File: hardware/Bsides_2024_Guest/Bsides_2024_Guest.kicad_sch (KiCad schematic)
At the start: 31 parts, among them J1 UART, J2 Battery, J3 OLED, J4 I2C, P1 USB_C_Plug_USB2.0, Q1 DMG3415U-7, SW1 ON, SW2 RESET, SW3 GPIO, SW4 RESET, SW5 RESET, SW6 RESET, SW7 RESET, U1 ESP32-C6-WROOM-1U-N4, U2 AP2112K-3.3

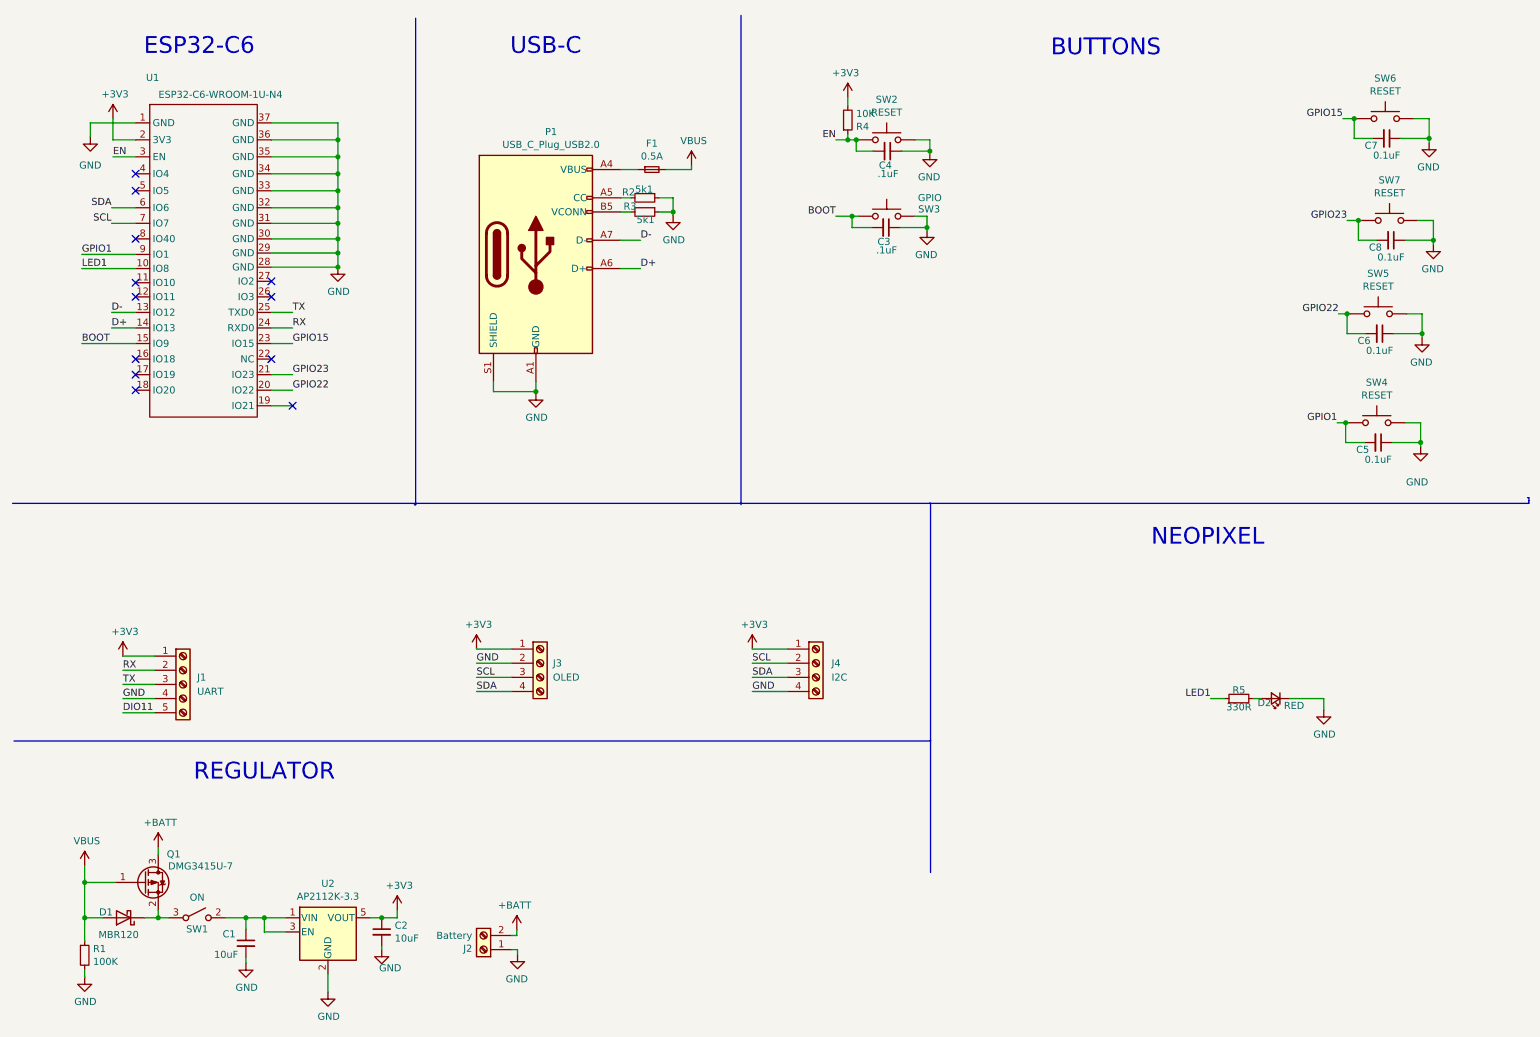
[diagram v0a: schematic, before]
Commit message: feat(Hw):Added_Guest_And_Sponsor_Floorplan_and_3d_Models
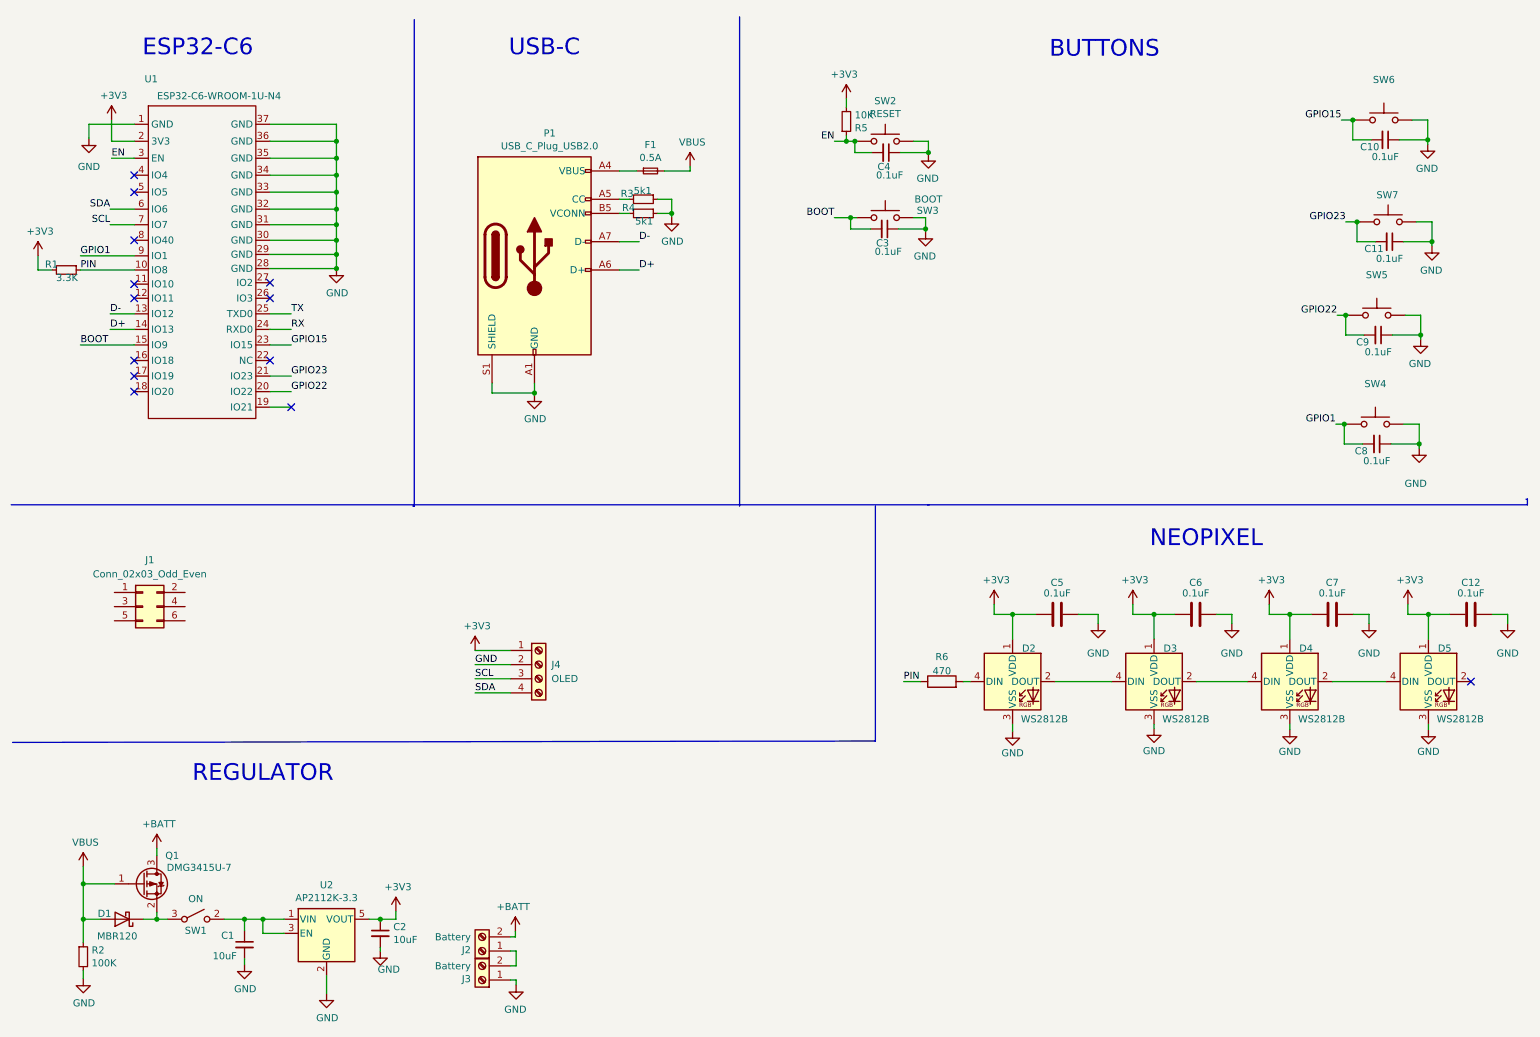
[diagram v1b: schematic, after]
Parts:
- removed C5, C6, C7: 0.1uF, symbol Device:C_Small
- removed D2: RED, LED_SMD:LED_0805_2012Metric, symbol Device:LED_Small
- removed J1: UART, Connector_PinHeader_2.54mm:PinHeader_1x05_P2.54mm_Vertical, symbol Connector:Screw_Terminal_01x05
- removed J3: OLED, Connector_PinHeader_2.54mm:PinHeader_1x04_P2.54mm_Vertical, symbol Connector:Screw_Terminal_01x04
- added C10, C11, C9: 0.1uF, Capacitor_SMD:C_0603_1608Metric, symbol Device:C_Small
- added C12, C5, C6, C7: 0.1uF, Capacitor_SMD:C_0603_1608Metric, symbol Device:C
- added D2, D3, D4, D5: WS2812B, LED_SMD:LED_WS2812B-Mini_PLCC4_3.5x3.5mm, symbol LED:WS2812B
- added J1: Conn_02x03_Odd_Even, Connector_PinSocket_2.54mm:PinSocket_2x03_P2.54mm_Vertical, symbol Connector_Generic:Conn_02x03_Odd_Even
- added J3: Battery, bsides:BH-AAA-A1aj001, symbol Connector:Screw_Terminal_01x02
- added R6: 470, Resistor_SMD:R_0603_1608Metric, symbol Device:R
- C3, C4: value .1uF -> 0.1uF
- C8: footprint (none) -> Capacitor_SMD:C_0603_1608Metric
- J2: footprint Footprint:BAT-TH_BH-AAA-A1AJ024 -> bsides:BH-AAA-A1aj001
- J4: value I2C -> OLED; footprint Connector_PinHeader_2.54mm:PinHeader_1x04_P2.54mm_Vertical -> bsides:Display OLED 128 x32; LCSC# C2691448 -> (none); manf# (none) -> I2C SH1106 Display Oled Azul 128×64 1.3 ”; provedor LCSC -> UNIT Electronics
- P1: footprint Footprint:C393939 -> bsides:C393939
- R1: value 100K -> 3.3K; LCSC# C25803 -> (none); Proveedor LCSC -> (none); provedor LCSC -> (none)
- R2: value 5k1 -> 100K; LCSC# C191782 -> C25803; Proveedor (none) -> LCSC; manf# ERJ3RBD5101V -> (none)
- R4: value 10K -> 5k1; LCSC# C217281 -> C191782; manf# CR-03JL7---10K -> ERJ3RBD5101V
- R5: value 330R -> 10K; footprint Resistor_SMD:R_0805_2012Metric_Pad1.20x1.40mm_HandSolder -> Resistor_SMD:R_0603_1608Metric; LCSC# C119075 -> C217281; manf# (none) -> CR-03JL7---10K
- SW1: footprint Footprint:JS102011SAQN -> bsides:MSK12C02
- SW3: value GPIO -> BOOT
- SW5, SW7: value RESET -> ~
- U1: footprint Footprint:MOD28_ESP32-C6-WROOM-1U_EXP -> bsides:XCVR_ESP32-C6-WROOM-1-N8
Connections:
- net +3V3: now also R1.2, R5.2, C12.2, C5.2, C6.2, C7.2, D2.1 (VDD), D3.1 (VDD), D4.1 (VDD), D5.1 (VDD); no longer R4.2
- net EN: now also R5.1; no longer R4.1
- net GND: now also J4.2 (Pin_2), R2.2, R4.1, C10.1, C11.1, C12.1, C5.1, C6.1, C7.1, C9.1, D2.3 (VSS), D3.3 (VSS), D4.3 (VSS), D5.3 (VSS), J3.1 (Pin_1); no longer J2.1 (Pin_1), J4.4 (Pin_4), R1.2, R2.1
- net GPIO1: now also C8.2
- net GPIO15: now also C10.2
- net GPIO22: now also C9.2
- net GPIO23: now also C11.2; no longer C8.2
- net SCL: now also J4.3 (Pin_3); no longer J4.2 (Pin_2)
- net SDA: now also J4.4 (Pin_4); no longer J4.3 (Pin_3)
- net VBUS: now also R2.1; no longer R1.1
- net at R3.2: now also P1.A5 (CC); no longer P1.B5 (VCONN)
- net LED1 renamed PIN
- net PIN: now also R1.1, R6.1; no longer R5.1
- new net: P1.B5 (VCONN), R4.2
- new net: D3.2 (DOUT), D4.4 (DIN)
- new net: D2.2 (DOUT), D3.4 (DIN)
- new net: J2.1 (Pin_1), J3.2 (Pin_2)
- new net: D4.2 (DOUT), D5.4 (DIN)
- new net: D2.4 (DIN), R6.2
- no-connect marks 12 -> 13

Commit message: feat(Hw): Shitty Addon PCB added
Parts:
- added C13: 1uF, Capacitor_SMD:C_0603_1608Metric, symbol Device:C_Small
- added C14, C15: 10uF, Capacitor_SMD:C_0603_1608Metric, symbol Device:C_Small
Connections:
- net +3V3: now also C13.1, C14.1, C15.1
- net GND: now also C13.2, C14.2, C15.2
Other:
- moved on the sheet: C3, C4, F1, P1, R3, R4, R5, SW2, SW3

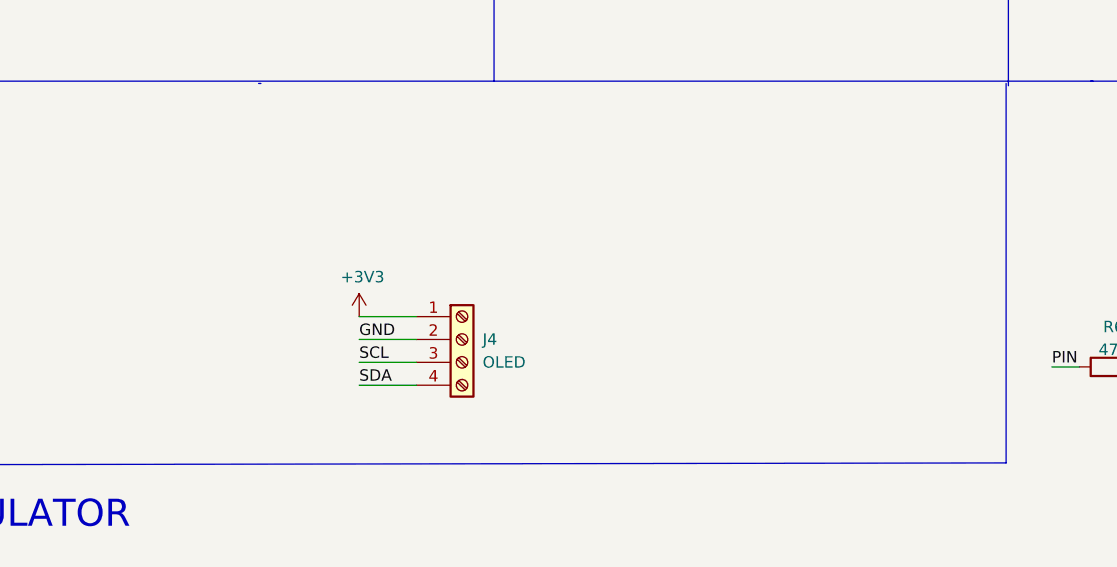
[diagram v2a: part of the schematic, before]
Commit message: feat(Hw): Start new floorplan
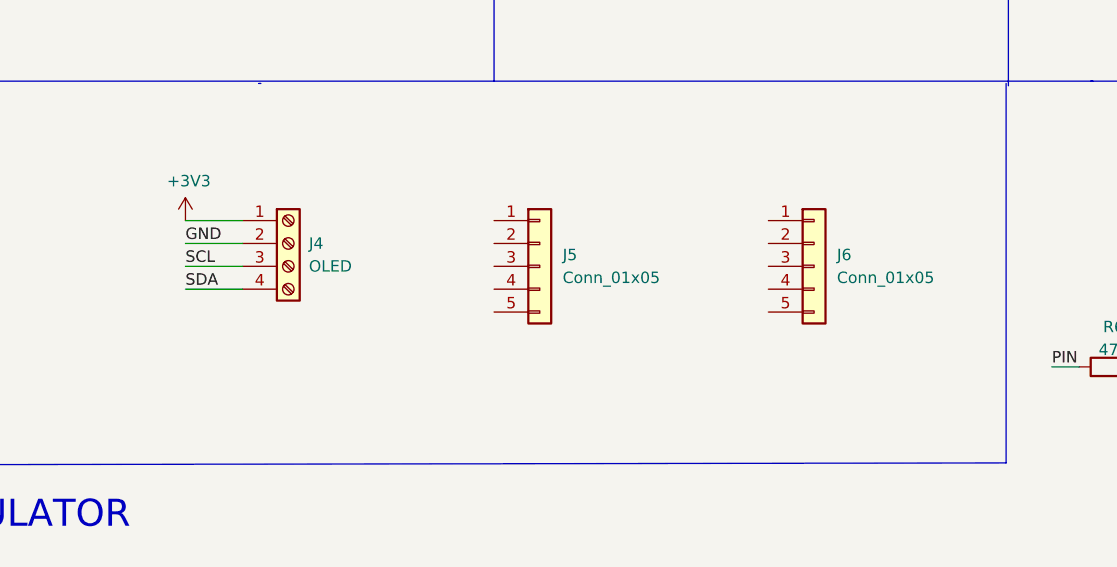
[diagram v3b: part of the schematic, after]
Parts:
- added J5, J6: Conn_01x05, Connector_PinHeader_2.54mm:PinHeader_1x05_P2.54mm_Vertical, symbol Connector_Generic:Conn_01x05
- J2, J3: footprint bsides:BH-AAA-A1aj001 -> Guest:BATT_8BH-AA-A1AJ020_MYG
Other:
- moved on the sheet: J4
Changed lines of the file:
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@@
 	(wire
 		(pts
-			(xy 95.504 126.238) (xy 101.854 126.238)
+			(xy 76.2 115.57) (xy 82.55 115.57)
 		)
 		(stroke
@@
 	(wire
 		(pts
-			(xy 95.504 128.778) (xy 101.854 128.778)
+			(xy 76.2 118.11) (xy 82.55 118.11)
 		)
 		(stroke
@@
 	(wire
 		(pts
-			(xy 95.504 131.318) (xy 101.854 131.318)
+			(xy 76.2 120.65) (xy 82.55 120.65)
 		)
 		(stroke
@@
 	(wire
 		(pts
-			(xy 95.504 133.858) (xy 101.854 133.858)
+			(xy 76.2 123.19) (xy 82.55 123.19)
 		)
 		(stroke
@@
 	)
 	(label "SDA"
-		(at 95.504 133.858 0)
+		(at 76.2 123.19 0)
 		(fields_autoplaced yes)
 		(effects
@@
 	)
 	(label "SCL"
-		(at 95.504 131.318 0)
+		(at 76.2 120.65 0)
 		(fields_autoplaced yes)
 		(effects
@@
 	)
 	(label "GND"
-		(at 95.504 128.778 0)
+		(at 76.2 118.11 0)
 		(fields_autoplaced yes)
 		(effects
@@
 	(symbol
 		(lib_id "Connector:Screw_Terminal_01x04")
-		(at 106.934 128.778 0)
+		(at 87.63 118.11 0)
 		(unit 1)
 		(exclude_from_sim no)
@@
 		(fields_autoplaced yes)
 		(property "Reference" "J4"
-			(at 109.22 128.7779 0)
+			(at 89.916 118.1099 0)
 			(effects
 				(font
@@
 		)
 		(property "Value" "OLED"
-			(at 109.22 131.3179 0)
+			(at 89.916 120.6499 0)
 			(effects
 				(font
@@
 		)
 		(property "Footprint" "bsides:Display OLED 128 x32"
-			(at 106.934 128.778 0)
+			(at 87.63 118.11 0)
 			(effects
 				(font
@@
 		)
 		(property "Datasheet" "~"
-			(at 106.934 128.778 0)
+			(at 87.63 118.11 0)
 			(effects
 				(font
@@
 		)
 		(property "Description" ""
-			(at 106.934 128.778 0)
+			(at 87.63 118.11 0)
 			(effects
 				(font
@@
 		)
 		(property "manf#" "I2C SH1106 Display Oled Azul 128×64 1.3 ” "
-			(at 106.934 128.778 0)
+			(at 87.63 118.11 0)
 			(effects
 				(font
@@
 		)
 		(property "provedor" "UNIT Electronics"
-			(at 106.934 128.778 0)
+			(at 87.63 118.11 0)
 			(effects
 				(font
@@
 	(symbol
 		(lib_id "power:+3V3")
-		(at 95.504 126.238 0)
+		(at 76.2 115.57 0)
 		(unit 1)
 		(exclude_from_sim no)
@@
 		(dnp no)
 		(property "Reference" "#PWR012"
-			(at 95.504 130.048 0)
+			(at 76.2 119.38 0)
 			(effects
 				(font
@@
 		)
 		(property "Value" "+3V3"
-			(at 95.885 121.8438 0)
+			(at 76.581 111.1758 0)
 			(effects
 				(font
@@
 		)
 		(property "Footprint" ""
-			(at 95.504 126.238 0)
+			(at 76.2 115.57 0)
 			(effects
 				(font
@@
 		)
 		(property "Datasheet" ""
-			(at 95.504 126.238 0)
+			(at 76.2 115.57 0)
 			(effects
 				(font
@@
 		)
 		(property "Description" ""
-			(at 95.504 126.238 0)
+			(at 76.2 115.57 0)
 			(effects
 				(font
@@
 			)
 		)
-		(property "Footprint" "bsides:BH-AAA-A1aj001"
+		(property "Footprint" "Guest:BATT_8BH-AA-A1AJ020_MYG"
 			(at 96.774 180.213 0)
 			(effects
@@
 	)
 	(symbol
+		(lib_id "Connector_Generic:Conn_01x05")
+		(at 146.05 120.65 0)
+		(unit 1)
+		(exclude_from_sim no)
+		(in_bom yes)
+		(on_board yes)
+		(dnp no)
+		(fields_autoplaced yes)
+		(property "Reference" "J6"
+			(at 148.59 119.3799 0)
+			(effects
+				(font
+					(size 1.27 1.27)
+				)
+				(justify left)
+			)
+		)
+		(property "Value" "Conn_01x05"
+			(at 148.59 121.9199 0)
+			(effects
+				(font
+					(size 1.27 1.27)
+				)
+				(justify left)
+			)
+		)
+		(property "Footprint" "Connector_PinHeader_2.54mm:PinHeader_1x05_P2.54mm_Vertical"
+			(at 146.05 120.65 0)
+			(effects
+				(font
+					(size 1.27 1.27)
+				)
+				(hide yes)
+			)
+		)
+		(property "Datasheet" "~"
+			(at 146.05 120.65 0)
+			(effects
+				(font
+					(size 1.27 1.27)
+				)
+				(hide yes)
+			)
+		)
+		(property "Description" "Generic connector, single row, 01x05, script generated (kicad-library-utils/schlib/autogen/connector/)"
+			(at 146.05 120.65 0)
+			(effects
+				(font
+					(size 1.27 1.27)
+				)
+				(hide yes)
+			)
+		)
+		(pin "1"
+		)
+		(pin "2"
+		)
+		(pin "4"
+		)
+		(pin "5"
+		)
+		(pin "3"
+		)
+		(instances
+			(project "Bsides_2024_Guest"
+				(path "/21a57a81-777f-4f81-b806-a7171bf6ef6c"
+					(reference "J6")
+					(unit 1)
+				)
+			)
+		)
+	)
+	(symbol
 		(lib_name "GND_11")
 		(lib_id "power:GND")
@@
 	)
 	(symbol
+		(lib_id "Connector_Generic:Conn_01x05")
+		(at 115.57 120.65 0)
+		(unit 1)
+		(exclude_from_sim no)
+		(in_bom yes)
+		(on_board yes)
+		(dnp no)
+		(fields_autoplaced yes)
+		(property "Reference" "J5"
+			(at 118.11 119.3799 0)
+			(effects
+				(font
+					(size 1.27 1.27)
+				)
+				(justify left)
+			)
+		)
+		(property "Value" "Conn_01x05"
+			(at 118.11 121.9199 0)
+			(effects
+				(font
+					(size 1.27 1.27)
+				)
+				(justify left)
+			)
+		)
+		(property "Footprint" "Connector_PinHeader_2.54mm:PinHeader_1x05_P2.54mm_Vertical"
+			(at 115.57 120.65 0)
+			(effects
+				(font
+					(size 1.27 1.27)
+				)
+				(hide yes)
+			)
+		)
+		(property "Datasheet" "~"
+			(at 115.57 120.65 0)
+			(effects
+				(font
+					(size 1.27 1.27)
+				)
+				(hide yes)
+			)
+		)
+		(property "Description" "Generic connector, single row, 01x05, script generated (kicad-library-utils/schlib/autogen/connector/)"
+			(at 115.57 120.65 0)
+			(effects
+				(font
+					(size 1.27 1.27)
+				)
+				(hide yes)
+			)
+		)
+		(pin "1"
+		)
+		(pin "2"
+		)
+		(pin "4"
+		)
+		(pin "5"
+		)
+		(pin "3"
+		)
+		(instances
+			(project "Bsides_2024_Guest"
+				(path "/21a57a81-777f-4f81-b806-a7171bf6ef6c"
+					(reference "J5")
+					(unit 1)
+				)
+			)
+		)
+	)
+	(symbol
 		(lib_id "Device:C_Small")
 		(at 100.33 65.278 0)
@@
 			)
 		)
-		(property "Footprint" "bsides:BH-AAA-A1aj001"
+		(property "Footprint" "Guest:BATT_8BH-AA-A1AJ020_MYG"
 			(at 96.774 185.42 0)
 			(effects

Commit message: feat(Hw): Update PCB
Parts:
- J1: value Conn_02x03_Odd_Even -> Add_On
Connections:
- net GND: now also J1.2 (Pin_2)
- net SCL: now also J1.4 (Pin_4)
- net SDA: now also J1.3 (Pin_3)
- net VBUS: now also C1.1, U2.1 (VIN), U2.3 (EN); no longer D1.2 (A), Q1.1 (G), R2.1
- net VOUT: now reaches J1.1 (Pin_1)
- net VOUT: now also C12.2, C13.1, C14.1, C15.1, C5.2, C6.2, C7.2, D2.1 (VDD), D3.1 (VDD), D4.1 (VDD), D5.1 (VDD), J4.1 (Pin_1), R1.2, R5.2, SW1.2 (B), U1.2 (3V3)
- removed net +3V3: C12.2, C13.1, C14.1, C15.1, C2.1, C5.2, C6.2, C7.2, D2.1 (VDD), D3.1 (VDD), D4.1 (VDD), D5.1 (VDD), J4.1 (Pin_1), R1.2, R5.2, U1.2 (3V3), U2.5 (VOUT)
- new net: C2.1, D1.2 (A), Q1.1 (G), R2.1, U2.5 (VOUT)
- no-connect marks 13 -> 15
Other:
- moved on the sheet: C1, C13, C14, C15, C2, C3, C4, D1, J1, J2, J3, Q1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
